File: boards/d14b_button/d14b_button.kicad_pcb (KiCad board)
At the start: 2 copper layers, 84 x 84 mm, 65 parts, among them CON1 USB-MICRO-B, P1 CONN_02X05, P2 CONN_01X03, P3 PIEZO_BUZZ, P4 EEPROM_SPI, Q1 MOSFET_N, Q2 IRLM6402, Q3 BSS138, SW1 SW_PUSH, SW2 SW_PUSH, SW3 SW_PUSH, SW4 SW_PUSH, U1 nRF24L01+-Module, U2 STM32F030C8T6, U3 TPS61221, X1 8M, X2 32.768k

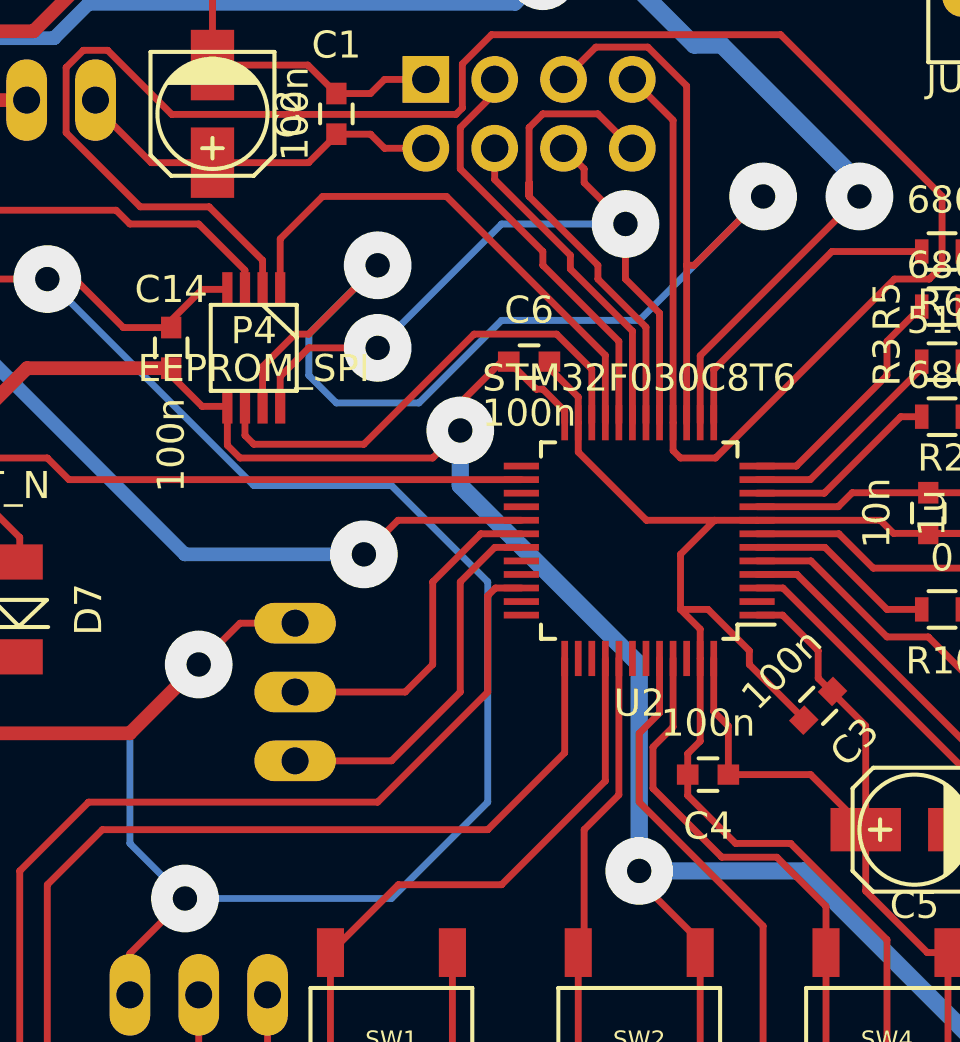
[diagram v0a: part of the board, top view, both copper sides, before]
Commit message: fix for mirrored right side of EEPROM
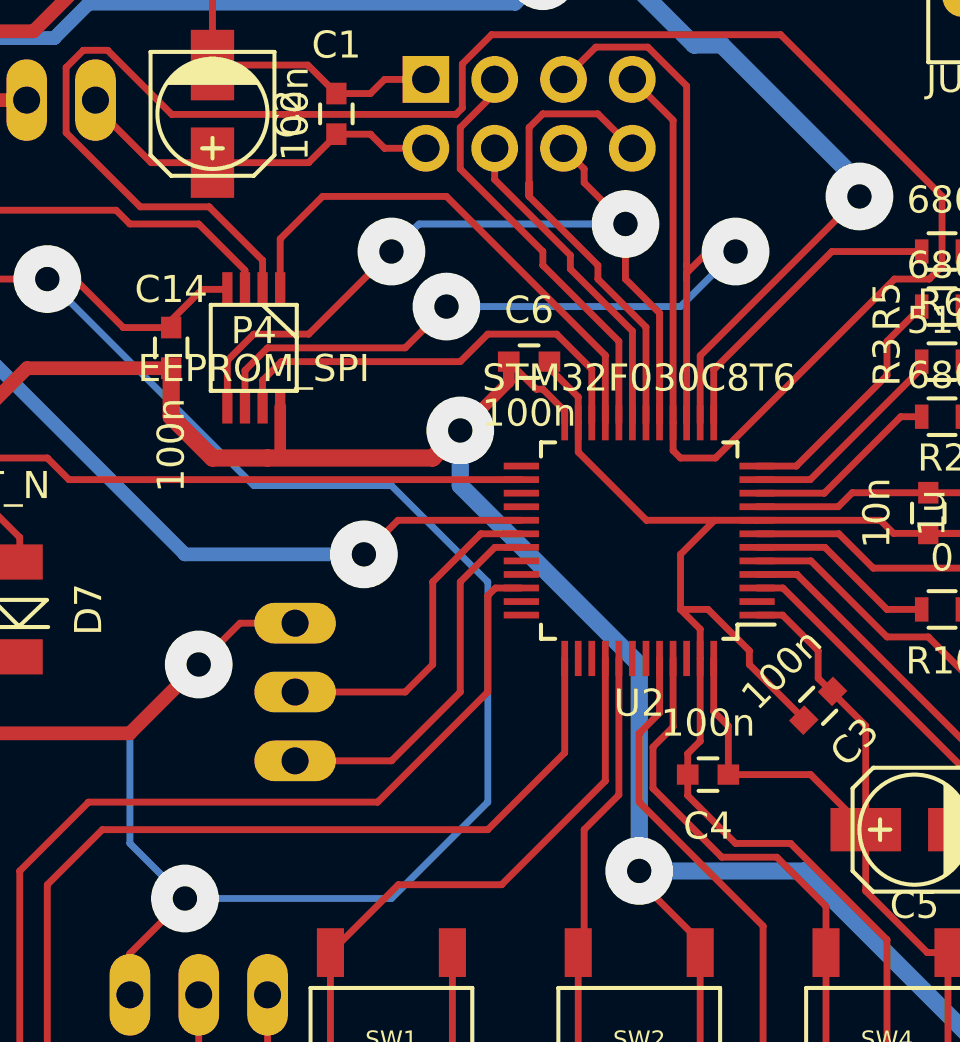
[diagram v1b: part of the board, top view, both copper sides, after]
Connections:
- P4 pad 5: +3V3 -> /MOSI
- P4 pad 6: /ROM_HOLD -> /SCK
- P4 pad 7: /SCK -> /ROM_HOLD
- P4 pad 8: /MOSI -> +3V3
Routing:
- net /SCK: track 54.7 -> 41.7 mm
- net +3V3: track 370.7 -> 373.5 mm
- net /MOSI: track 27.8 -> 30.1 mm
- net /ROM_HOLD: track 18.2 -> 16.3 mm

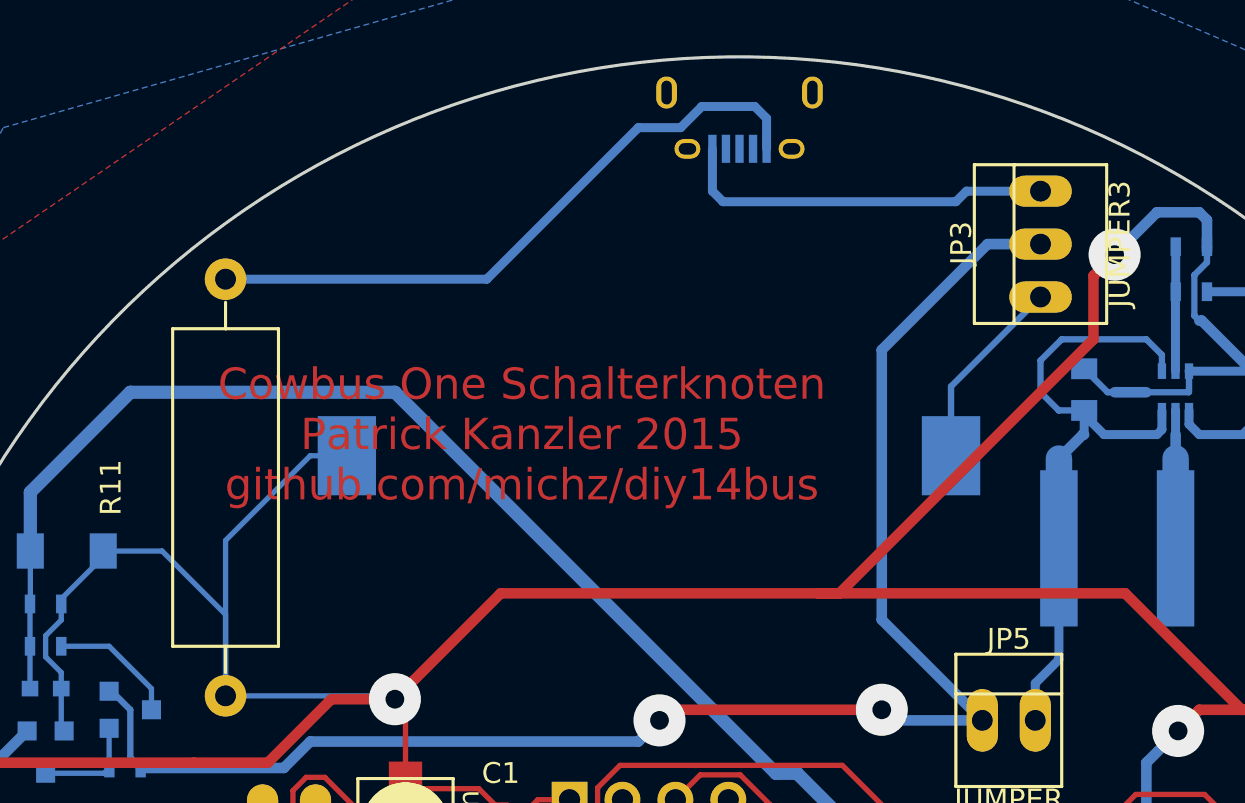
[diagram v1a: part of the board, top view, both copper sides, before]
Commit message: Spannungswandler für USB hinzugefügt
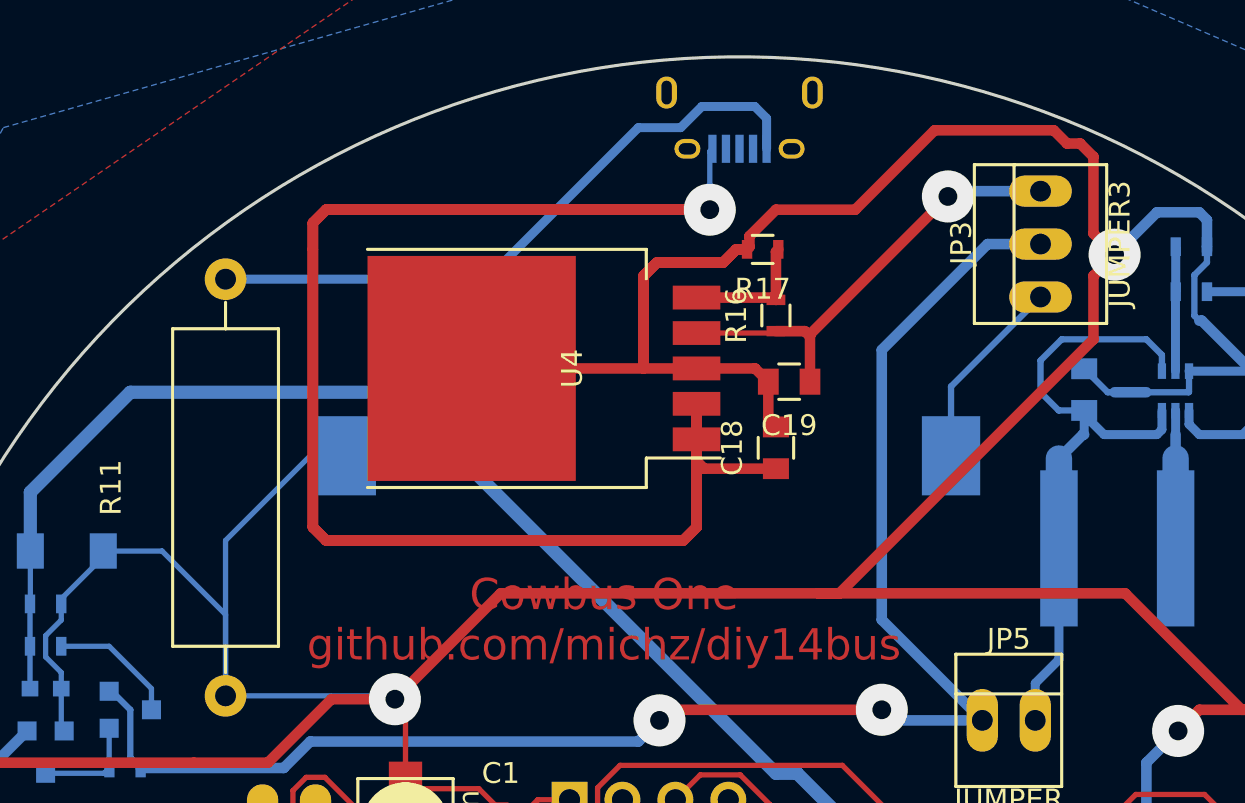
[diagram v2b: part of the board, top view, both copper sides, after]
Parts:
- added C18: 10u, Capacitors_SMD:C_0805, F.Cu at (154.9, 81.9)
- added C19: 10u, Capacitors_SMD:C_0805, F.Cu at (155.6, 78.7)
- added R16: *, Resistors_SMD:R_0603, F.Cu at (154.9, 75.6)
- added R17: *, Resistors_SMD:R_0603, F.Cu at (154.3, 72.4)
- added U4: LP38502-ADJ, SMD_Packages:TO-263-5, F.Cu at (151.1, 78.1)
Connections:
- CON1 pad 1: Net-(CON1-Pad1) -> Net-(C18-Pad1)
- CON1 pad 2: (no net) -> Net-(CON1-Pad2)
- CON1 pad 3: (no net) -> Net-(CON1-Pad3)
- CON1 pad 4: (no net) -> Net-(CON1-Pad4)
- CON1 pad 6: (no net) -> Net-(CON1-Pad6)
- CON1 pad 7: (no net) -> Net-(CON1-Pad7)
- CON1 pad 8: (no net) -> Net-(CON1-Pad8)
- CON1 pad 9: (no net) -> Net-(CON1-Pad9)
- JP3 pad 3: Net-(CON1-Pad1) -> Net-(C19-Pad1)
- P1 pad 6: (no net) -> Net-(P1-Pad6)
- P1 pad 7: (no net) -> Net-(P1-Pad7)
- P1 pad 8: (no net) -> Net-(P1-Pad8)
- P1 pad 9: (no net) -> Net-(P1-Pad9)
- U2 pad 2: (no net) -> Net-(U2-Pad2)
- U2 pad 25: (no net) -> Net-(U2-Pad25)
- U2 pad 27: (no net) -> Net-(U2-Pad27)
- U2 pad 28: (no net) -> Net-(U2-Pad28)
- U2 pad 32: (no net) -> Net-(U2-Pad32)
- U2 pad 33: (no net) -> Net-(U2-Pad33)
- U2 pad 35: (no net) -> Net-(U2-Pad35)
- U2 pad 36: (no net) -> Net-(U2-Pad36)
- U2 pad 38: (no net) -> Net-(U2-Pad38)
- U2 pad 39: (no net) -> Net-(U2-Pad39)
- U2 pad 42: (no net) -> Net-(U2-Pad42)
- U2 pad 43: (no net) -> Net-(U2-Pad43)
- U2 pad 46: (no net) -> Net-(U2-Pad46)
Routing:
- net Net-(C18-Pad1): track 0.00 -> 127.0 mm, vias 0 -> 1
- net GND: track 590.9 -> 658.1 mm
- net Net-(C19-Pad1): track 0.00 -> 23.5 mm, vias 0 -> 1
- net Net-(CON1-Pad1): track 18.2 -> 0.00 mm
- net Net-(R16-Pad2): track 0.00 -> 6.33 mm
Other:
- board text added: "Cowbus One github.com/michz/diy14bus"
- board text removed: "Cowbus One Schalterknoten Patrick Kanzler 2015 github.com/michz/diy14bus"
